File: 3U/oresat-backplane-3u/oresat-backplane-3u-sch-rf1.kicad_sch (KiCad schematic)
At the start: 30 parts

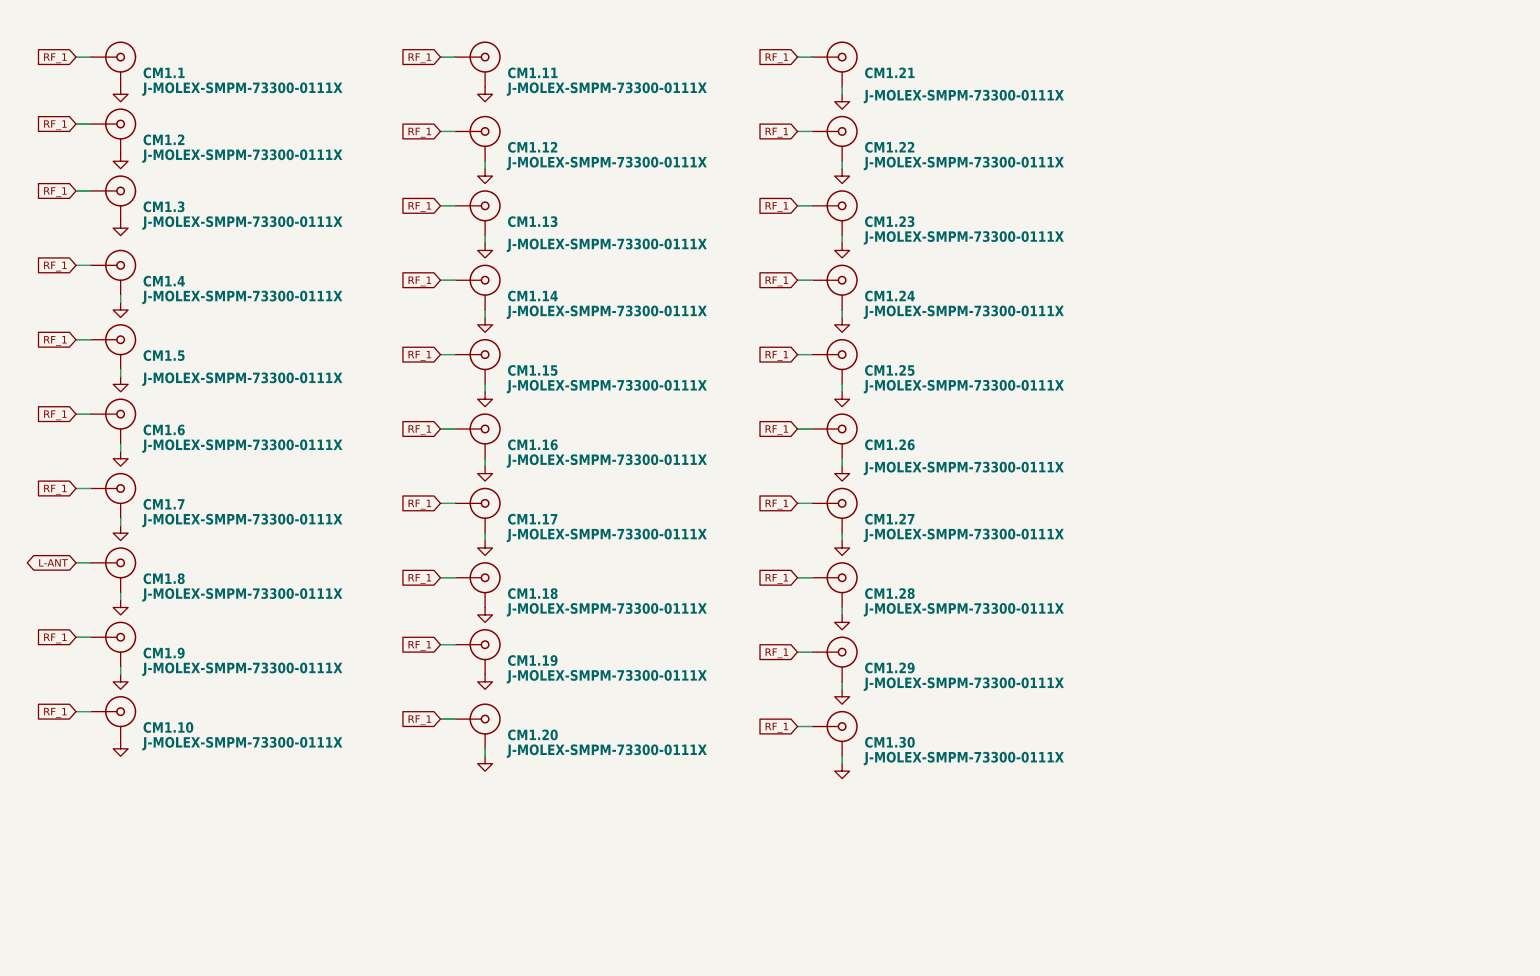
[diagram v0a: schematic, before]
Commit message: Moved can lines to back & fixed RF schematic organization
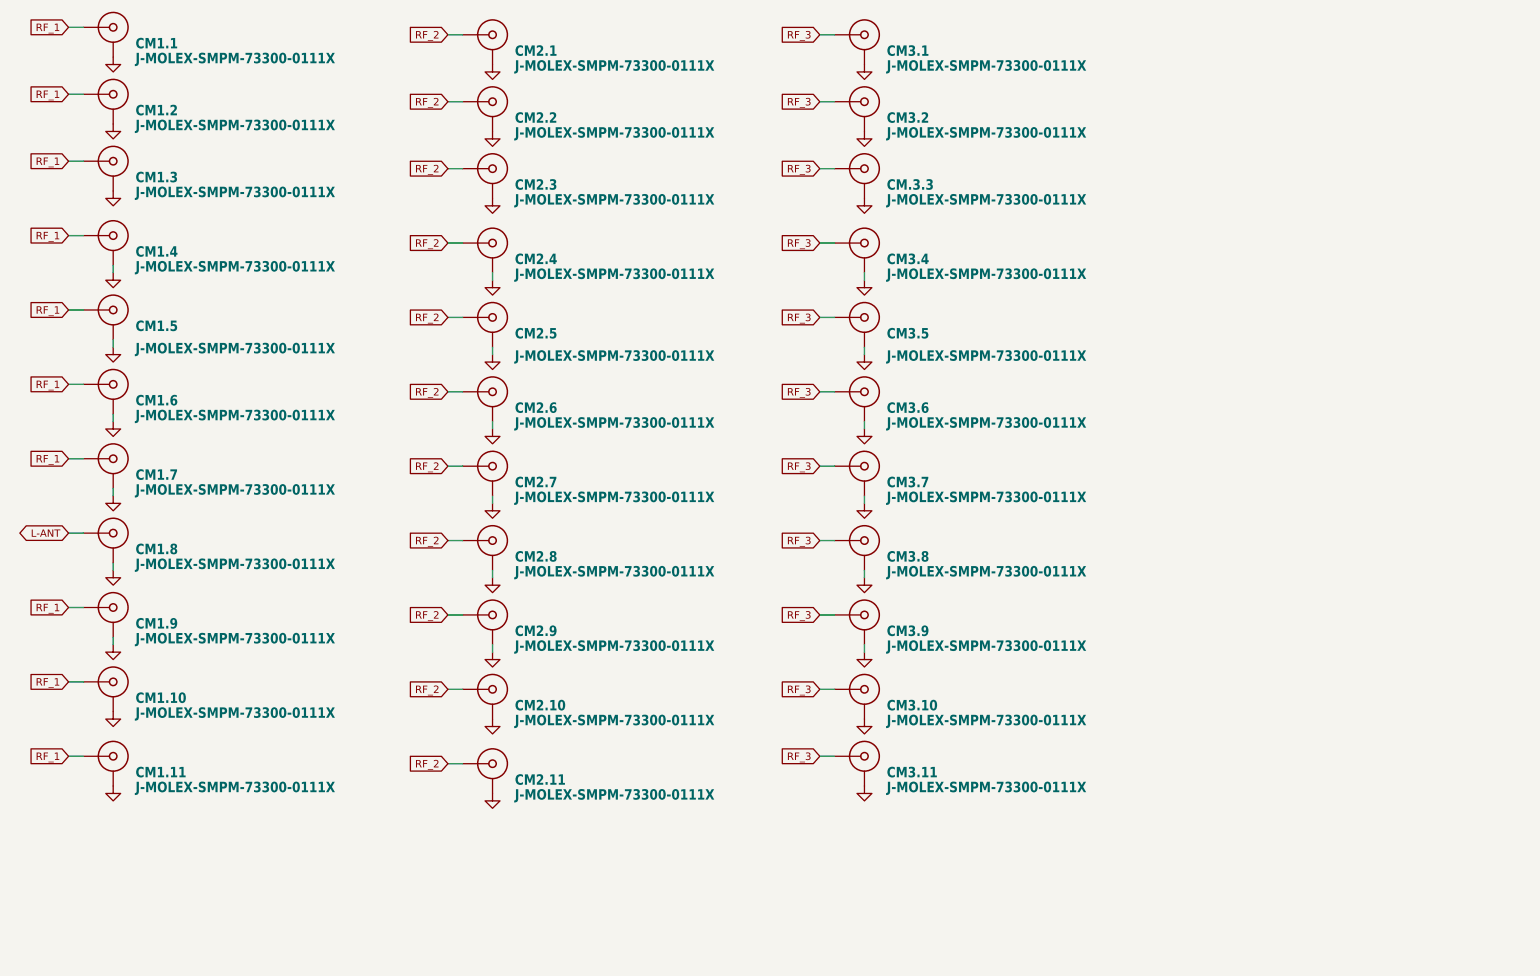
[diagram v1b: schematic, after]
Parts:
- removed CM1.12, CM1.13, CM1.14, CM1.15, CM1.16, CM1.17, CM1.18, CM1.19, CM1.20, CM1.21, CM1.22, CM1.23, CM1.24, CM1.25, CM1.26, CM1.27, CM1.28, CM1.29, CM1.30: J-MOLEX-SMPM-73300-0111X, oresat-connectors:J-MOLEX-SMPM-73300-0111X-long, symbol oresat-connectors:J-MOLEX-SMPM-73300-0111X_1
- added CM.3.3, CM2.1, CM2.10, CM2.11, CM2.2, CM2.3, CM2.4, CM2.5, CM2.6, CM2.7, CM2.8, CM2.9, CM3.1, CM3.10, CM3.11, CM3.2, CM3.4, CM3.5, CM3.6, CM3.7, CM3.8, CM3.9: J-MOLEX-SMPM-73300-0111X, oresat-connectors:J-MOLEX-SMPM-73300-0111X-long, symbol oresat-connectors:J-MOLEX-SMPM-73300-0111X_1
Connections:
- net GND: now also CM.3.3.GND (SHIELD1), CM2.1.GND (SHIELD1), CM2.10.GND (SHIELD1), CM2.11.GND (SHIELD1), CM2.2.GND (SHIELD1), CM2.3.GND (SHIELD1), CM2.4.GND (SHIELD1), CM2.5.GND (SHIELD1), CM2.6.GND (SHIELD1), CM2.7.GND (SHIELD1), CM2.8.GND (SHIELD1), CM2.9.GND (SHIELD1), CM3.1.GND (SHIELD1), CM3.10.GND (SHIELD1), CM3.11.GND (SHIELD1), CM3.2.GND (SHIELD1), CM3.4.GND (SHIELD1), CM3.5.GND (SHIELD1), CM3.6.GND (SHIELD1), CM3.7.GND (SHIELD1), CM3.8.GND (SHIELD1), CM3.9.GND (SHIELD1)
- new net RF_2: CM2.1.RF-DOWN (RF), CM2.10.RF-DOWN (RF), CM2.11.RF-DOWN (RF), CM2.2.RF-DOWN (RF), CM2.3.RF-DOWN (RF), CM2.4.RF-DOWN (RF), CM2.5.RF-DOWN (RF), CM2.6.RF-DOWN (RF), CM2.7.RF-DOWN (RF), CM2.8.RF-DOWN (RF), CM2.9.RF-DOWN (RF)
- new net RF_3: CM.3.3.RF-DOWN (RF), CM3.1.RF-DOWN (RF), CM3.10.RF-DOWN (RF), CM3.11.RF-DOWN (RF), CM3.2.RF-DOWN (RF), CM3.4.RF-DOWN (RF), CM3.5.RF-DOWN (RF), CM3.6.RF-DOWN (RF), CM3.7.RF-DOWN (RF), CM3.8.RF-DOWN (RF), CM3.9.RF-DOWN (RF)
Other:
- moved on the sheet: CM1.1, CM1.10, CM1.11, CM1.2, CM1.3, CM1.4, CM1.5, CM1.6, CM1.7, CM1.8, CM1.9

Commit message: Updated generic 3U backplane with correct fastener copper and solder mask cutouts under fastners, and updated date on sch and brd.
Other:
- company: (none) -> Portland State Aerospace Society
- title: (none) -> Generic OreSat 3U Backplane
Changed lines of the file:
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@@
 	(generator "eeschema")
 	(generator_version "9.0")
-	(paper "A4")
+	(paper "B")
+	(title_block
+		(title "Generic OreSat 3U Backplane")
+		(date "2026-02-20")
+		(rev "1.0")
+		(company "Portland State Aerospace Society")
+	)
 	(wire
 		(pts

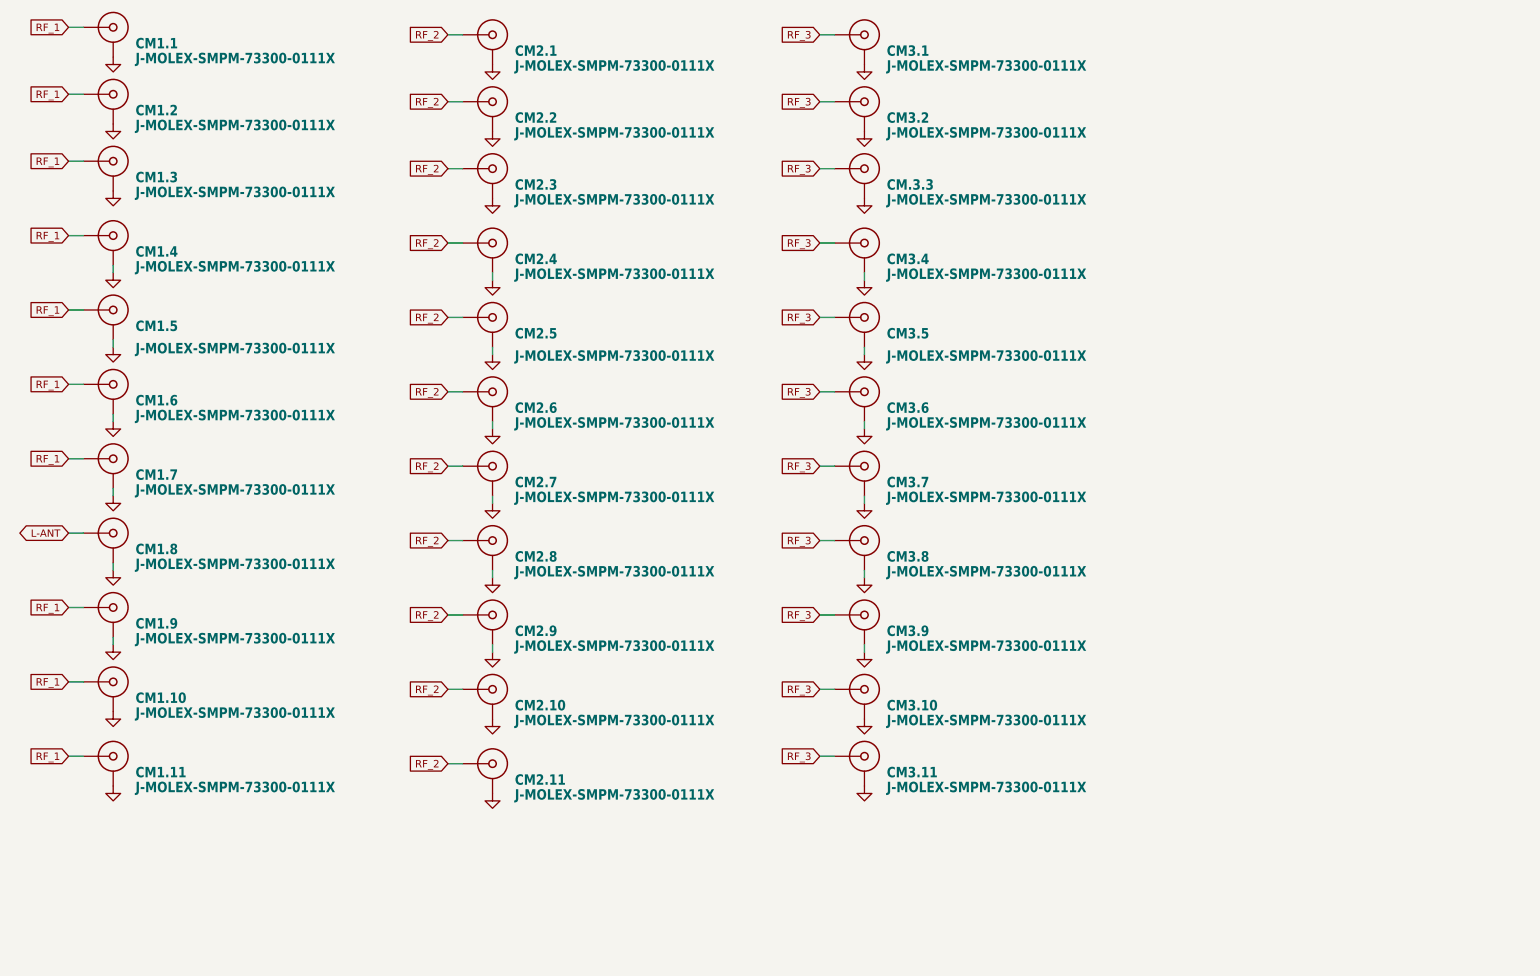
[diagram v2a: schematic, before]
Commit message: Connected Spares and switched OPD to inner layer. Updated RF cons -- **RF con new footprint has ground pad schematic parity error
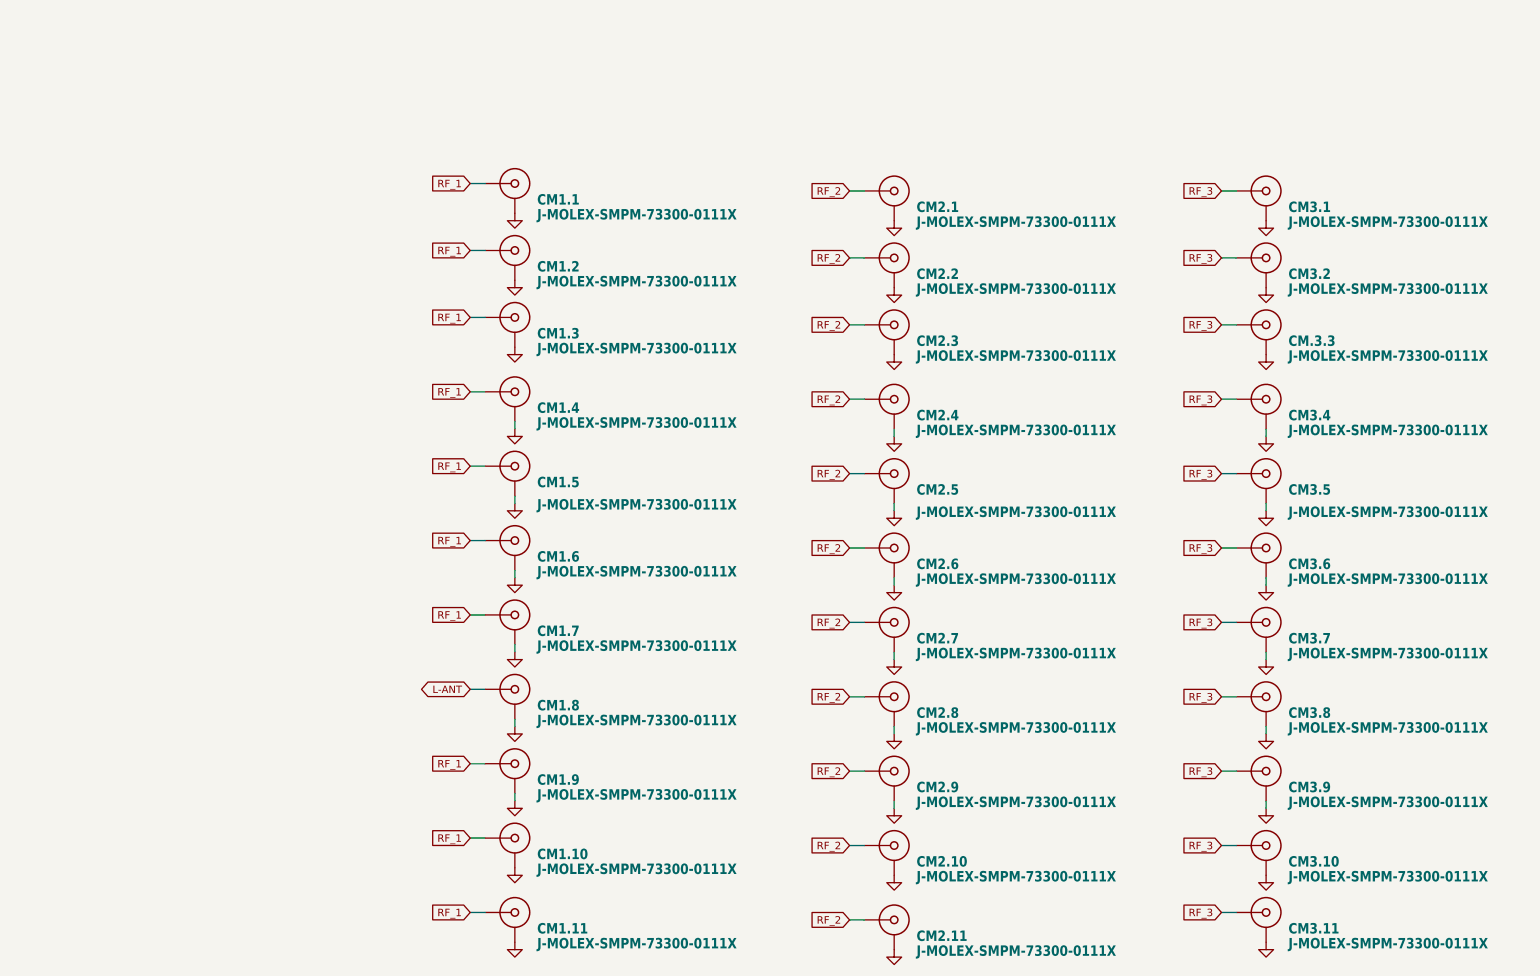
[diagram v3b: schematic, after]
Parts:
- CM.3.3, CM1.1, CM1.10, CM1.11, CM1.2, CM1.3, CM1.4, CM1.5, CM1.6, CM1.7, CM1.8, CM1.9, CM2.1, CM2.10, CM2.11, CM2.2, CM2.3, CM2.4, CM2.5, CM2.6, CM2.7, CM2.8, CM2.9, CM3.1, CM3.10, CM3.11, CM3.2, CM3.4, CM3.5, CM3.6, CM3.7, CM3.8, CM3.9: footprint oresat-connectors:J-MOLEX-SMPM-73300-0111X-long -> oresat-connectors:J-MOLEX-SMPM-73300-011X
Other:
- moved on the sheet: CM.3.3, CM1.1, CM1.10, CM1.11, CM1.2, CM1.3, CM1.4, CM1.5, CM1.6, CM1.7, CM1.8, CM1.9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

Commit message: Updated schematic symbol for RF con. Believe this is done. Remaining DRC errors are only unconnected RF cons -- fine until use defined for non-generic version.
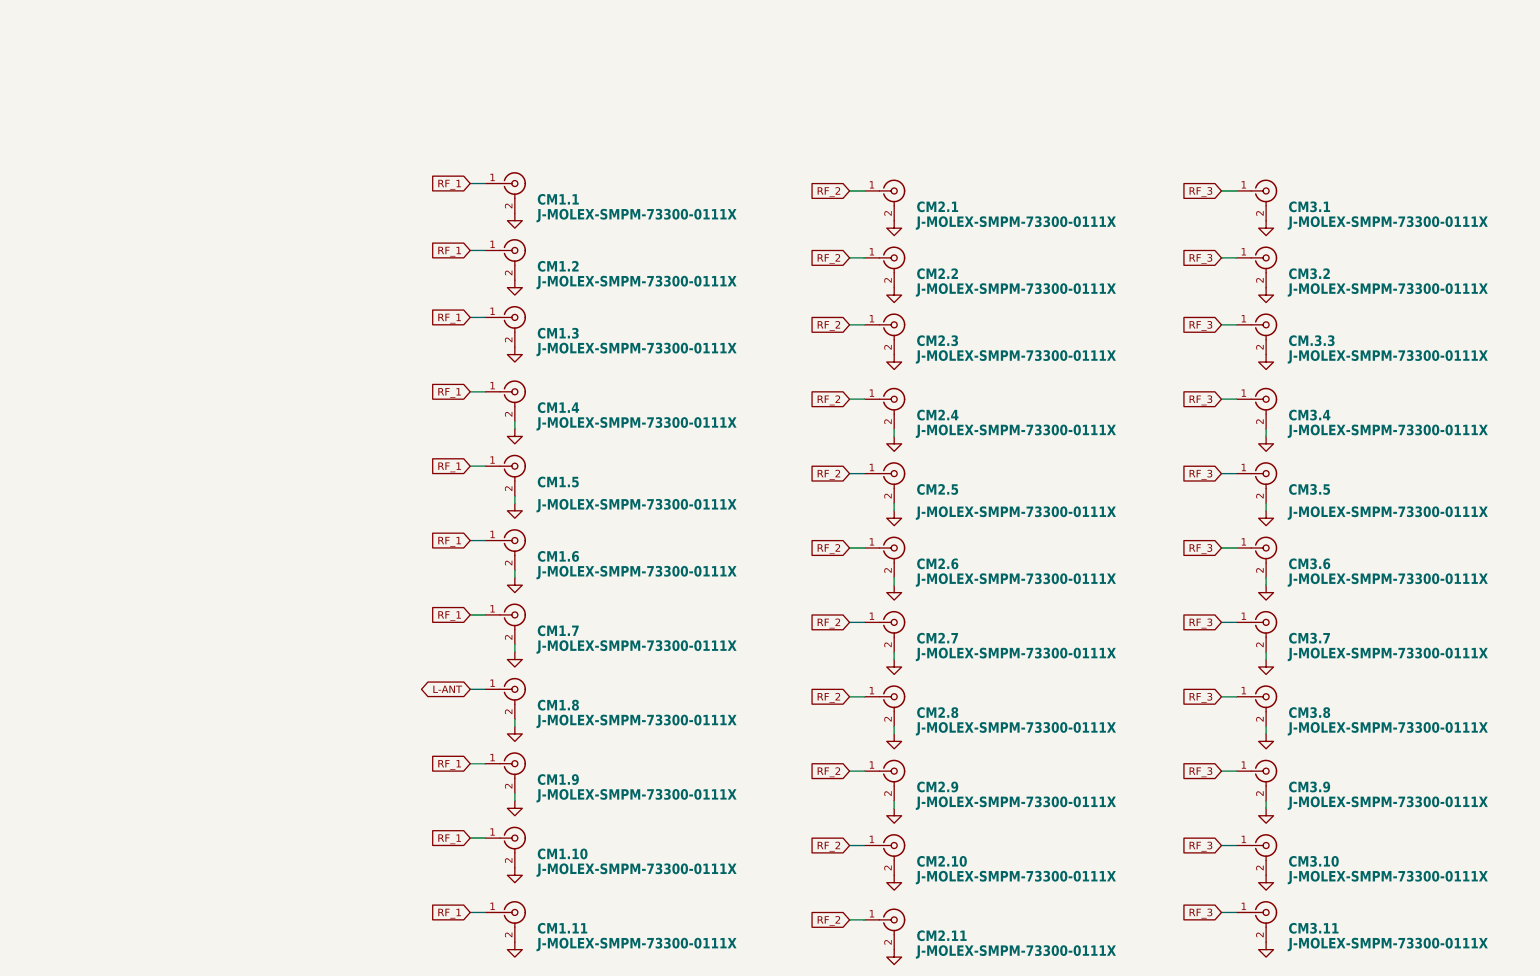
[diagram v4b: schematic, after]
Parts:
- CM.3.3, CM1.1, CM1.10, CM1.11, CM1.2, CM1.3, CM1.4, CM1.5, CM1.6, CM1.7, CM1.8, CM1.9, CM2.1, CM2.10, CM2.11, CM2.2, CM2.3, CM2.4, CM2.5, CM2.6, CM2.7, CM2.8, CM2.9, CM3.1, CM3.10, CM3.11, CM3.2, CM3.4, CM3.5, CM3.6, CM3.7, CM3.8, CM3.9: symbol oresat-connectors:J-MOLEX-SMPM-73300-0111X_1 -> Connector:Conn_Coaxial
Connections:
- net GND: now also CM.3.3.2 (Ext), CM1.1.2 (Ext), CM1.10.2 (Ext), CM1.11.2 (Ext), CM1.2.2 (Ext), CM1.3.2 (Ext), CM1.4.2 (Ext), CM1.5.2 (Ext), CM1.6.2 (Ext), CM1.7.2 (Ext), CM1.8.2 (Ext), CM1.9.2 (Ext), CM2.1.2 (Ext), CM2.10.2 (Ext), CM2.11.2 (Ext), CM2.2.2 (Ext), CM2.3.2 (Ext), CM2.4.2 (Ext), CM2.5.2 (Ext), CM2.6.2 (Ext), CM2.7.2 (Ext), CM2.8.2 (Ext), CM2.9.2 (Ext), CM3.1.2 (Ext), CM3.10.2 (Ext), CM3.11.2 (Ext), CM3.2.2 (Ext), CM3.4.2 (Ext), CM3.5.2 (Ext), CM3.6.2 (Ext), CM3.7.2 (Ext), CM3.8.2 (Ext), CM3.9.2 (Ext); no longer CM.3.3.GND (SHIELD1), CM1.1.GND (SHIELD1), CM1.10.GND (SHIELD1), CM1.11.GND (SHIELD1), CM1.2.GND (SHIELD1), CM1.3.GND (SHIELD1), CM1.4.GND (SHIELD1), CM1.5.GND (SHIELD1), CM1.6.GND (SHIELD1), CM1.7.GND (SHIELD1), CM1.8.GND (SHIELD1), CM1.9.GND (SHIELD1), CM2.1.GND (SHIELD1), CM2.10.GND (SHIELD1), CM2.11.GND (SHIELD1), CM2.2.GND (SHIELD1), CM2.3.GND (SHIELD1), CM2.4.GND (SHIELD1), CM2.5.GND (SHIELD1), CM2.6.GND (SHIELD1), CM2.7.GND (SHIELD1), CM2.8.GND (SHIELD1), CM2.9.GND (SHIELD1), CM3.1.GND (SHIELD1), CM3.10.GND (SHIELD1), CM3.11.GND (SHIELD1), CM3.2.GND (SHIELD1), CM3.4.GND (SHIELD1), CM3.5.GND (SHIELD1), CM3.6.GND (SHIELD1), CM3.7.GND (SHIELD1), CM3.8.GND (SHIELD1), CM3.9.GND (SHIELD1)
- net L-ANT: now also CM1.8.1 (In); no longer CM1.8.RF-DOWN (RF)
- net RF_1: now also CM1.1.1 (In), CM1.10.1 (In), CM1.11.1 (In), CM1.2.1 (In), CM1.3.1 (In), CM1.4.1 (In), CM1.5.1 (In), CM1.6.1 (In), CM1.7.1 (In), CM1.9.1 (In); no longer CM1.1.RF-DOWN (RF), CM1.10.RF-DOWN (RF), CM1.11.RF-DOWN (RF), CM1.2.RF-DOWN (RF), CM1.3.RF-DOWN (RF), CM1.4.RF-DOWN (RF), CM1.5.RF-DOWN (RF), CM1.6.RF-DOWN (RF), CM1.7.RF-DOWN (RF), CM1.9.RF-DOWN (RF)
- net RF_2: now also CM2.1.1 (In), CM2.10.1 (In), CM2.11.1 (In), CM2.2.1 (In), CM2.3.1 (In), CM2.4.1 (In), CM2.5.1 (In), CM2.6.1 (In), CM2.7.1 (In), CM2.8.1 (In), CM2.9.1 (In); no longer CM2.1.RF-DOWN (RF), CM2.10.RF-DOWN (RF), CM2.11.RF-DOWN (RF), CM2.2.RF-DOWN (RF), CM2.3.RF-DOWN (RF), CM2.4.RF-DOWN (RF), CM2.5.RF-DOWN (RF), CM2.6.RF-DOWN (RF), CM2.7.RF-DOWN (RF), CM2.8.RF-DOWN (RF), CM2.9.RF-DOWN (RF)
- net RF_3: now also CM.3.3.1 (In), CM3.1.1 (In), CM3.10.1 (In), CM3.11.1 (In), CM3.2.1 (In), CM3.4.1 (In), CM3.5.1 (In), CM3.6.1 (In), CM3.7.1 (In), CM3.8.1 (In), CM3.9.1 (In); no longer CM.3.3.RF-DOWN (RF), CM3.1.RF-DOWN (RF), CM3.10.RF-DOWN (RF), CM3.11.RF-DOWN (RF), CM3.2.RF-DOWN (RF), CM3.4.RF-DOWN (RF), CM3.5.RF-DOWN (RF), CM3.6.RF-DOWN (RF), CM3.7.RF-DOWN (RF), CM3.8.RF-DOWN (RF), CM3.9.RF-DOWN (RF)
